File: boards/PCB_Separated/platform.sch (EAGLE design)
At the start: 21 parts, among them IC1 FT232RL, U1 STM32F10XRXT6, X1 32khz, X8 8mhz

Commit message: -delete a useless sch pics -add ecu io pins diagram -add a GND to VSS line on FTDI. Hopefully internally connected with other GND pins -progress new separated ecu board.
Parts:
- added C-ICU1, C-TPS: 100n, resistor:C-EU050-024X044
- added IC2: L293D, st-microelectronics:L293D
- added L-ICU, L-IPWR, L-RUN: (no value), led:LED3MM
- added OK-ICU: H11L1M, optocoupler:H11L1M
- added Q1, Q2, Q3, Q4: IRF530, transistor-power:IRF530
- added R-FETA1, R-FETA2, R-FETA3, R-FETA4, R-ICU3, R-ICU4, R-IPWR, R-RUN: 330, resistor:R-EU_0204/7
- added R-FETB1, R-FETB2, R-FETB3, R-FETB4, R-FETC1, R-FETC2, R-FETC3, R-FETC4, R-ICU2, R-ICU5: 4k7, resistor:R-EU_0204/7
- added R-ICU1, R-RX, R-TPS1, R-TPS2, R-TX: 1k, resistor:R-EU_0204/7
- added TR-ICU: (no value), transistor-neu-to92:2N3904-NPN-TO92-EBC
- added X2: PN61729-S, con-berg:PN61729-S
- OK1: value H11L1M -> ILQ1; device optocoupler:H11L1M -> optocoupler:ILQ1
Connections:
- new net GND: OK1A.EMIT, OK1B.EMIT, OK1C.EMIT, OK1D.EMIT, Q1.S, Q2.S, Q3.S, Q4.S
- new net IGN1: Q3.D, R-FETC3.2
- new net IGN2: Q4.D, R-FETC4.2
- new net INJ1: Q1.D, R-FETC1.2
- new net INJ2: Q2.D, R-FETC2.2
- new net N$1: R-TPS1.1
- new net N$11: OK1A.COL, Q1.G, R-FETB1.2
- new net N$12: OK1B.A, R-FETA2.1
- new net N$13: OK1A.A, R-FETA1.1
- new net N$14: OK1C.COL, Q3.G, R-FETB3.2
- new net N$15: OK1C.A, R-FETA3.1
- new net N$16: OK1D.COL, Q4.G, R-FETB4.2
- new net N$17: OK1D.A, R-FETA4.1
- new net N$2: OK1B.COL, Q2.G, R-FETB2.2
- new net N$3: C-ICU1.1, R-ICU1.2, R-ICU2.2, TR-ICU.B
- new net N$4: L-ICU.C, OK-ICU.C, TR-ICU.C
- new net N$5: OK-ICU.A, R-ICU4.1
- new net N$6: L-ICU.A, R-ICU3.1
- new net N$7: L-IPWR.A, R-IPWR.1
- new net N$8: L-RUN.A, R-RUN.1
- new net N$9: R-ICU1.1
- new net V12: R-FETB1.1, R-FETB2.1, R-FETB3.1, R-FETB4.1, R-FETC1.1, R-FETC2.1, R-FETC3.1, R-FETC4.1
- net DM: now also X2.2
- net DP: now also X2.3
- net P14: now also C-TPS.1, R-TPS1.2, R-TPS2.2
- net P23: now also OK-ICU.OUT, R-ICU5.2
- net P37: now also OK1D.C
- net P38: now also OK1C.C
- net P39: now also OK1B.C
- net P40: now also OK1A.C
- net P41: now also L-RUN.C
- net P42: now also R-TX.1
- net P43: now also R-RX.1
- net RX: now also R-TX.2
- net TX: now also R-RX.2
- net VCC: now also X2.1
- net VDD: now also OK-ICU.VCC, R-FETA1.2, R-FETA2.2, R-FETA3.2, R-FETA4.2, R-ICU3.2, R-ICU4.2, R-ICU5.1, R-IPWR.2, R-RUN.2
- net VSS: now also C-ICU1.2, C-TPS.2, IC1.GND@2, L-IPWR.C, OK-ICU.GND, R-ICU2.1, R-TPS2.1, TR-ICU.E, X2.4, X2.S1, X2.S2

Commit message: progress to build new ecu boards
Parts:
- removed X8: 8mhz, crystal:CRYSTALHC49U-V
- added C-V12, C-VCC, C-VDD1: 100n/25v, resistor:CPOL-EUE2-5
- added C-VDD2: 100n, resistor:C-EU050-024X044
- added D-V12: 1N4004, diode:1N4004
- added IC3: (no value), v-reg:LM317TS
- added OK2: ILQ1, optocoupler:ILQ1
- added R-IACA1, R-IACA2, R-IACA3, R-IACA4, R-VDD1: 330, resistor:R-EU_0204/7
- added R-IACB1, R-IACB2, R-IACB3, R-IACB4: 4k7, resistor:R-EU_0204/7
- added R-VDD2: 270, resistor:R-EU_0204/7
- added X0: PN61729-S, con-berg:PN61729-S
- added X3, X4: (no value), con-subd:F09HP
- C-NRST: value (none) -> 100n
- IC2: value L293D -> 7805TV; device st-microelectronics:L293D -> linear:7805TV
- X2: value PN61729-S -> 8mhz; device con-berg:PN61729-S -> crystal:CRYSTALHC49U-V
- renumbered C-ICU1 to C-ICU, C1 to C-NRST, D1 to D-V33
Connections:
- removed net N$1: R-TPS1.1
- removed net N$9: R-ICU1.1
- new net IACA: OK2A.COL, R-IACB1.2, X4.8
- new net IACB: OK2B.COL, R-IACB2.2, X4.4
- new net IACC: OK2C.COL, R-IACB3.2, X4.9
- new net IACD: OK2D.COL, R-IACB4.2, X4.5
- new net ICU: R-ICU1.1, X3.2
- new net N$10: OK2A.A, R-IACA1.1
- new net N$18: OK2B.A, R-IACA2.1
- new net N$21: OK2C.A, R-IACA3.1
- new net N$22: OK2D.A, R-IACA4.1
- new net N$25: IC3.ADJ, R-VDD1.2, R-VDD2.1
- new net TPS: R-TPS1.1, X3.3
- net DM: now also X0.2; no longer X2.2
- net DP: now also X0.3; no longer X2.3
- net GND: now also C-V12.-, D-V12.C, OK2A.EMIT, OK2B.EMIT, OK2C.EMIT, OK2D.EMIT, X3.5
- net IGN1: now also X4.2
- net IGN2: now also X4.7
- net INJ1: now also X4.1
- net INJ2: now also X4.6
- net P33: now also OK2D.C
- net P34: now also OK2C.C
- net P35: now also OK2B.C
- net P36: now also OK2A.C
- net P5: now also X2.2; no longer X8.2
- net P6: now also X2.1; no longer X8.1
- net V12: now also C-V12.+, IC2.VI, IC3.IN, R-IACB1.1, R-IACB2.1, R-IACB3.1, R-IACB4.1, X3.9
- net VCC: now also C-VCC.+, IC2.VO, X0.1, X3.8; no longer X2.1
- net VDD: now also C-VDD1.+, C-VDD2.2, IC3.OUT, R-IACA1.2, R-IACA2.2, R-IACA3.2, R-IACA4.2, R-VDD2.2
- net VSS: now also C-VCC.-, C-VDD1.-, C-VDD2.1, D-V12.A, IC2.GND, R-VDD1.1, X0.4, X0.S1, X0.S2, X3.4, X3.7; no longer X2.4, X2.S1, X2.S2

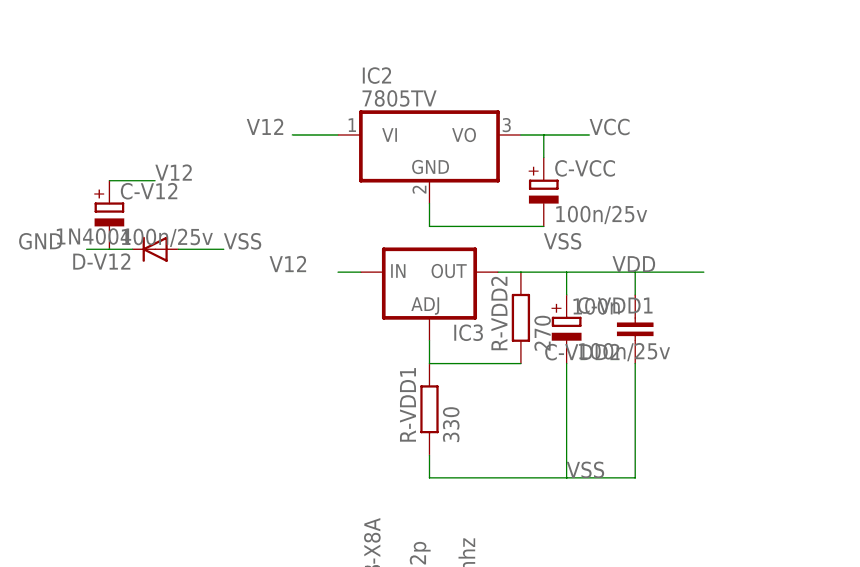
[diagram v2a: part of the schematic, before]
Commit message: add connector board
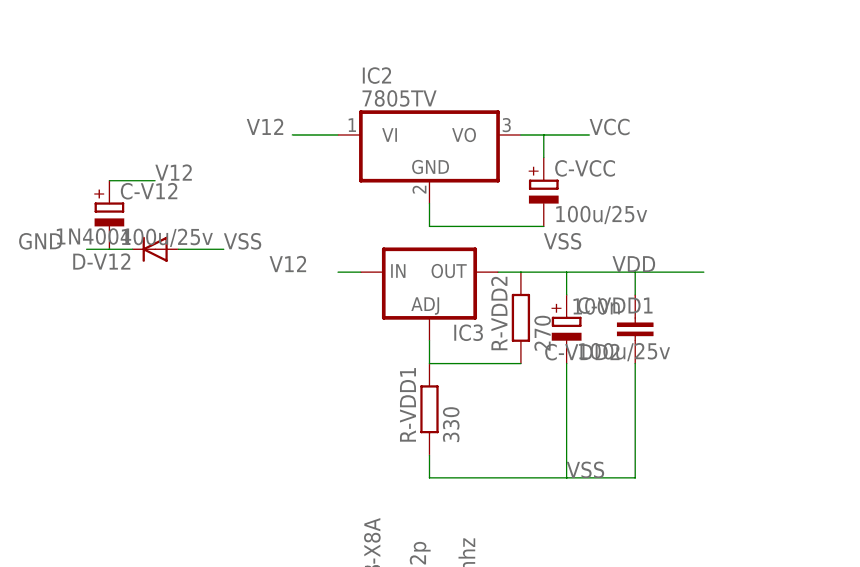
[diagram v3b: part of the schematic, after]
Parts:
- C-V12, C-VCC, C-VDD1: value 100n/25v -> 100u/25v
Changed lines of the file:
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@@
 <part name="R-VDD1" library="resistor" deviceset="R-EU_" device="0204/7" value="330"/>
 <part name="R-VDD2" library="resistor" deviceset="R-EU_" device="0204/7" value="270"/>
-<part name="C-V12" library="resistor" deviceset="CPOL-EU" device="E2-5" value="100n/25v"/>
+<part name="C-V12" library="resistor" deviceset="CPOL-EU" device="E2-5" value="100u/25v"/>
 <part name="D-V12" library="diode" deviceset="1N4004" device=""/>
-<part name="C-VCC" library="resistor" deviceset="CPOL-EU" device="E2-5" value="100n/25v"/>
-<part name="C-VDD1" library="resistor" deviceset="CPOL-EU" device="E2-5" value="100n/25v"/>
+<part name="C-VCC" library="resistor" deviceset="CPOL-EU" device="E2-5" value="100u/25v"/>
+<part name="C-VDD1" library="resistor" deviceset="CPOL-EU" device="E2-5" value="100u/25v"/>
 <part name="C-VDD2" library="resistor" deviceset="C-EU" device="050-024X044" value="100n"/>
 <part name="X3" library="con-subd" deviceset="F09HP" device=""/>
